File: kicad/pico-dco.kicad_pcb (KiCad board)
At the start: 2 copper layers, 1 part, among them U1 Pico

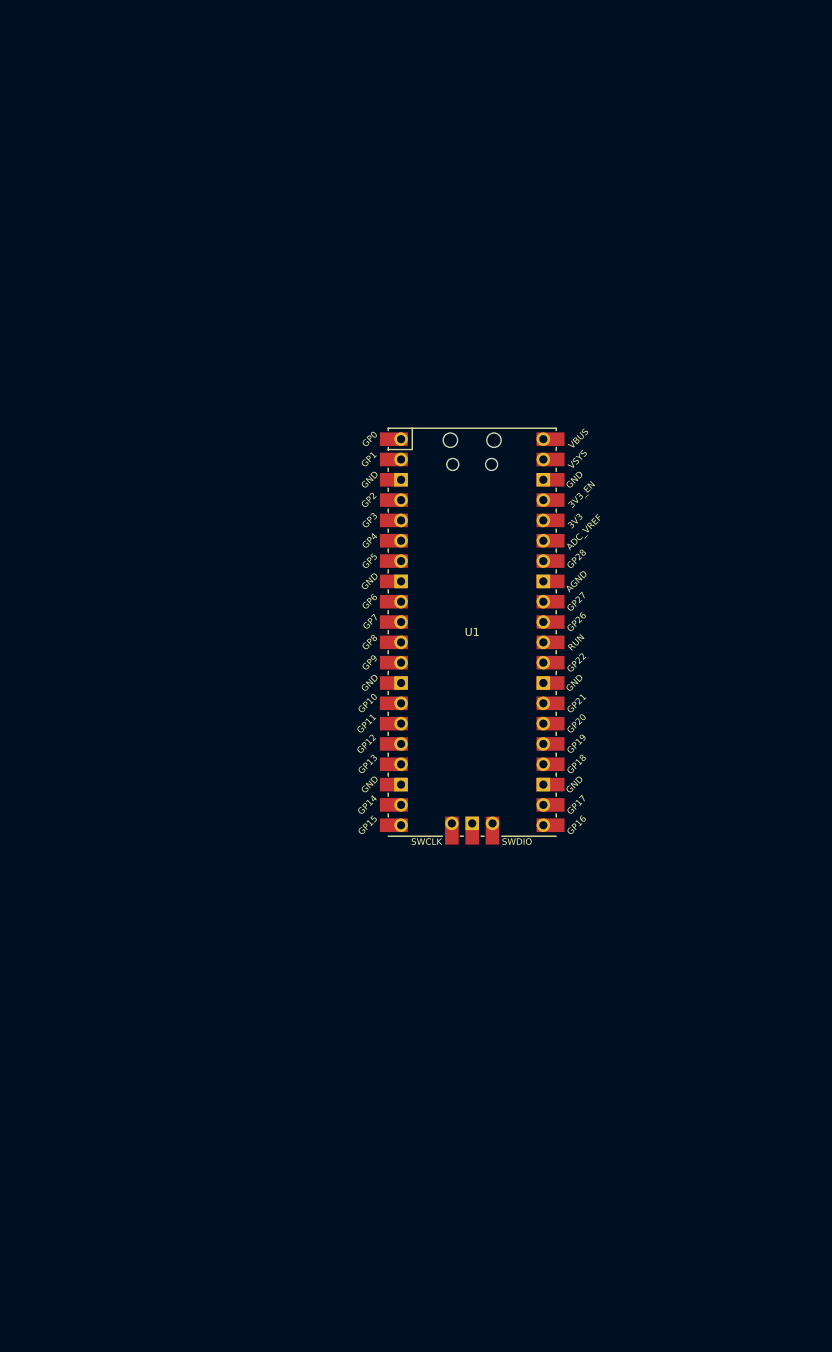
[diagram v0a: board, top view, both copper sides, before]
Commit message: Add 6 voices and serial midi to kicad schematics/PCB
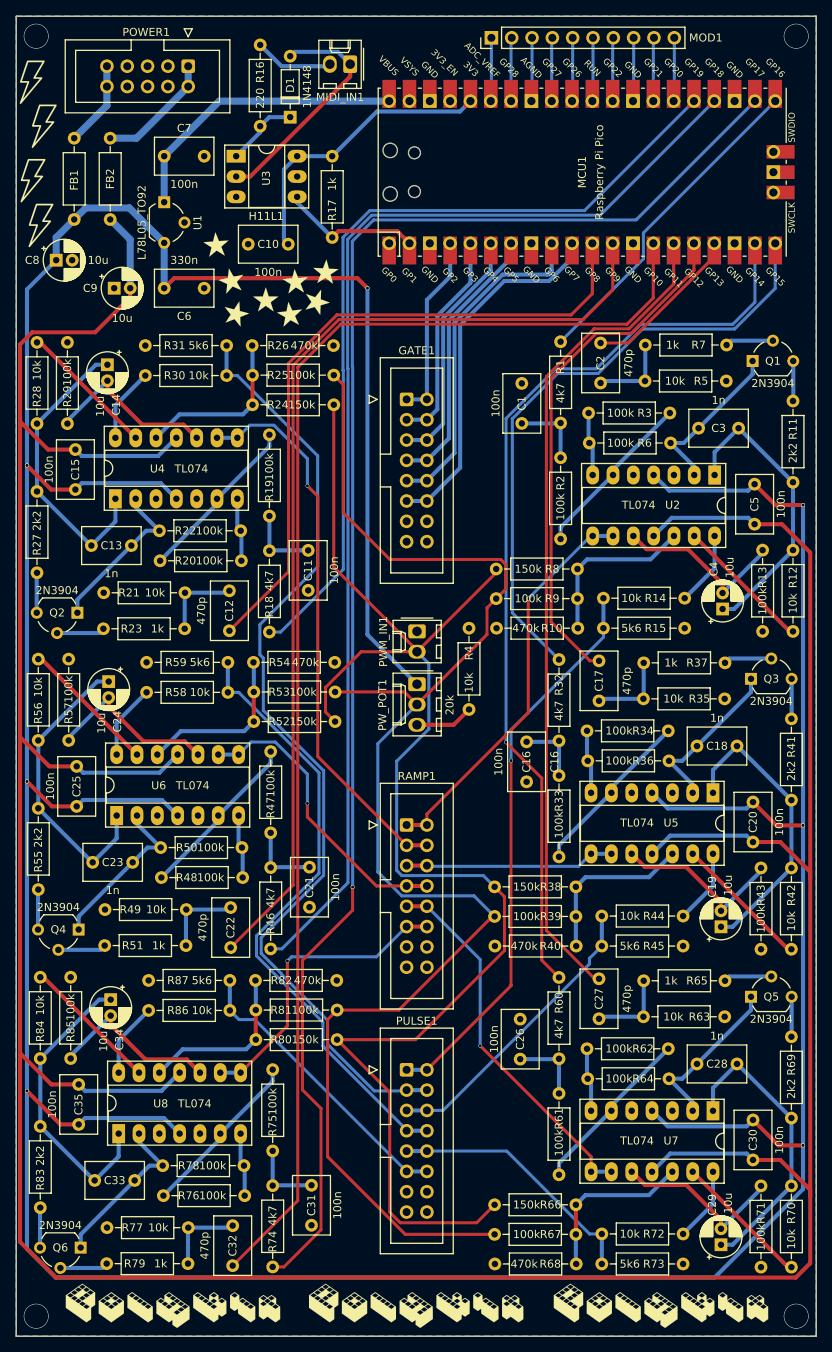
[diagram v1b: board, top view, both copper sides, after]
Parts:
- added C1: 100n, Capacitor_THT:C_Rect_L7.2mm_W4.5mm_P5.00mm_FKS2_FKP2_MKS2_MKP2, F.Cu at (113.2, 70.9)
- added C10: 100n, Capacitor_THT:C_Rect_L7.2mm_W4.5mm_P5.00mm_FKS2_FKP2_MKS2_MKP2, F.Cu at (84.0, 48.5)
- added C11: 100n, Capacitor_THT:C_Rect_L7.2mm_W4.5mm_P5.00mm_FKS2_FKP2_MKS2_MKP2, F.Cu at (86.5, 86.8)
- added C12: 470p, Capacitor_THT:C_Rect_L7.2mm_W4.5mm_P5.00mm_FKS2_FKP2_MKS2_MKP2, F.Cu at (76.7, 91.8)
- added C13: 1n, Capacitor_THT:C_Rect_L7.2mm_W4.5mm_P5.00mm_FKS2_FKP2_MKS2_MKP2, F.Cu at (59.4, 86.2)
- added C14: 10u, Capacitor_THT:CP_Radial_D5.0mm_P2.00mm, F.Cu at (61.4, 63.6)
- added C15: 100n, Capacitor_THT:C_Rect_L7.2mm_W4.5mm_P5.00mm_FKS2_FKP2_MKS2_MKP2, F.Cu at (57.4, 79.2)
- added C16: 100n, Capacitor_THT:C_Rect_L7.2mm_W4.5mm_P5.00mm_FKS2_FKP2_MKS2_MKP2, F.Cu at (113.8, 110.7)
- added C17: 470p, Capacitor_THT:C_Rect_L7.2mm_W4.5mm_P5.00mm_FKS2_FKP2_MKS2_MKP2, F.Cu at (122.8, 105.6)
- added C18: 1n, Capacitor_THT:C_Rect_L7.2mm_W4.5mm_P5.00mm_FKS2_FKP2_MKS2_MKP2, F.Cu at (140.1, 111.2)
- added C19: 10u, Capacitor_THT:CP_Radial_D5.0mm_P2.00mm, F.Cu at (138.1, 133.8)
- added C2: 470p, Capacitor_THT:C_Rect_L7.2mm_W4.5mm_P5.00mm_FKS2_FKP2_MKS2_MKP2, F.Cu at (123.0, 65.8)
- added C20: 100n, Capacitor_THT:C_Rect_L7.2mm_W4.5mm_P5.00mm_FKS2_FKP2_MKS2_MKP2, F.Cu at (142.1, 118.2)
- added C21: 100n, Capacitor_THT:C_Rect_L7.2mm_W4.5mm_P5.00mm_FKS2_FKP2_MKS2_MKP2, F.Cu at (86.7, 126.4)
- added C22: 470p, Capacitor_THT:C_Rect_L7.2mm_W4.5mm_P5.00mm_FKS2_FKP2_MKS2_MKP2, F.Cu at (76.8, 131.4)
- added C23: 1n, Capacitor_THT:C_Rect_L7.2mm_W4.5mm_P5.00mm_FKS2_FKP2_MKS2_MKP2, F.Cu at (59.6, 125.8)
- added C24: 10u, Capacitor_THT:CP_Radial_D5.0mm_P2.00mm, F.Cu at (61.6, 103.2)
- added C25: 100n, Capacitor_THT:C_Rect_L7.2mm_W4.5mm_P5.00mm_FKS2_FKP2_MKS2_MKP2, F.Cu at (57.6, 118.8)
- added C26: 100n, Capacitor_THT:C_Rect_L7.2mm_W4.5mm_P5.00mm_FKS2_FKP2_MKS2_MKP2, F.Cu at (113.0, 150.4)
- added C27: 470p, Capacitor_THT:C_Rect_L7.2mm_W4.5mm_P5.00mm_FKS2_FKP2_MKS2_MKP2, F.Cu at (122.8, 145.3)
- added C28: 1n, Capacitor_THT:C_Rect_L7.2mm_W4.5mm_P5.00mm_FKS2_FKP2_MKS2_MKP2, F.Cu at (140.1, 151.0)
- added C29: 10u, Capacitor_THT:CP_Radial_D5.0mm_P2.00mm, F.Cu at (138.1, 173.6)
- added C3: 1n, Capacitor_THT:C_Rect_L7.2mm_W4.5mm_P5.00mm_FKS2_FKP2_MKS2_MKP2, F.Cu at (140.3, 71.5)
- added C30: 100n, Capacitor_THT:C_Rect_L7.2mm_W4.5mm_P5.00mm_FKS2_FKP2_MKS2_MKP2, F.Cu at (142.1, 158.0)
- added C31: 100n, Capacitor_THT:C_Rect_L7.2mm_W4.5mm_P5.00mm_FKS2_FKP2_MKS2_MKP2, F.Cu at (86.9, 166.1)
- added C32: 470p, Capacitor_THT:C_Rect_L7.2mm_W4.5mm_P5.00mm_FKS2_FKP2_MKS2_MKP2, F.Cu at (77.1, 171.2)
- added C33: 1n, Capacitor_THT:C_Rect_L7.2mm_W4.5mm_P5.00mm_FKS2_FKP2_MKS2_MKP2, F.Cu at (59.8, 165.5)
- added C34: 10u, Capacitor_THT:CP_Radial_D5.0mm_P2.00mm, F.Cu at (61.8, 142.9)
- added C35: 100n, Capacitor_THT:C_Rect_L7.2mm_W4.5mm_P5.00mm_FKS2_FKP2_MKS2_MKP2, F.Cu at (57.8, 158.5)
- added C4: 10u, Capacitor_THT:CP_Radial_D5.0mm_P2.00mm, F.Cu at (138.3, 94.1)
- added C5: 100n, Capacitor_THT:C_Rect_L7.2mm_W4.5mm_P5.00mm_FKS2_FKP2_MKS2_MKP2, F.Cu at (142.3, 78.5)
- added C6: 330n, Capacitor_THT:C_Rect_L7.2mm_W4.5mm_P5.00mm_FKS2_FKP2_MKS2_MKP2, F.Cu at (73.5, 54.0)
- added C7: 100n, Capacitor_THT:C_Rect_L7.2mm_W4.5mm_P5.00mm_FKS2_FKP2_MKS2_MKP2, F.Cu at (68.5, 37.5)
- added C8: 10u, Capacitor_THT:CP_Radial_D5.0mm_P2.00mm, F.Cu at (55.0, 50.5)
- added C9: 10u, Capacitor_THT:CP_Radial_D5.0mm_P2.00mm, F.Cu at (62.2, 54.0)
- added D1: 1N4148, Diode_THT:D_DO-35_SOD27_P7.62mm_Horizontal, F.Cu at (84.2, 32.6)
- added FB1: Ferrite_Bead, Resistor_THT:R_Axial_DIN0207_L6.3mm_D2.5mm_P10.16mm_Horizontal, F.Cu at (57.2, 35.2)
- added FB2: Ferrite_Bead, Resistor_THT:R_Axial_DIN0207_L6.3mm_D2.5mm_P10.16mm_Horizontal, F.Cu at (61.8, 35.2)
- added G***: LOGO, Polykit:star-silk-tiny, F.Cu at (75.0, 48.5)
- added G***: LOGO, Polykit:blitz-silk-tiny, F.Cu at (52.1, 40.6)
- added G***: LOGO, Polykit:blitz-silk-tiny, F.Cu at (53.5, 33.8)
- added G***: LOGO, Polykit:blitz-silk-tiny, F.Cu at (52.0, 28.3)
- added G***: LOGO, Polykit:bär-small, B.Cu at (93.2, 38.7)
- added G***: LOGO, Polykit:logo-silk-2.5cm, F.Cu at (100.0, 181.2)
- added G***: LOGO, Polykit:logo-silk-2.5cm, F.Cu at (130.6, 181.2)
- added G***: LOGO, Polykit:logo-silk-2.5cm, F.Cu at (69.6, 181.2)
- added G***: LOGO, Polykit:star-silk-tiny, F.Cu at (76.9, 53.0)
- added G***: LOGO, Polykit:star-silk-tiny, F.Cu at (77.5, 57.1)
- added G***: LOGO, Polykit:star-silk-tiny, F.Cu at (81.2, 55.4)
- added G***: LOGO, Polykit:star-silk-tiny, F.Cu at (84.9, 53.1)
- added G***: LOGO, Polykit:star-silk-tiny, F.Cu at (84.2, 57.2)
- added G***: LOGO, Polykit:star-silk-tiny, F.Cu at (87.6, 55.6)
- added G***: LOGO, Polykit:star-silk-tiny, F.Cu at (88.7, 51.9)
- added G***: LOGO, Polykit:blitz-silk-tiny, F.Cu at (53.1, 46.2)
- added GATE1: Conn_02x08_Odd_Even, Connector_IDC:IDC-Header_2x08_P2.54mm_Vertical, F.Cu at (98.8, 67.9)
- added MCU1: Raspberry Pi Pico, RPi_Pico:RPi_Pico_SMD_TH, F.Cu at (120.8, 39.5)
- added MIDI_IN1: Conn_01x02, Connector_Molex:Molex_KK-254_AE-6410-02A_1x02_P2.54mm_Vertical, F.Cu at (91.8, 26.0)
- added MOD1: Conn_01x10, Connector_PinHeader_2.54mm:PinHeader_1x10_P2.54mm_Vertical, F.Cu at (109.4, 22.7)
- added POWER1: Conn_02x05_Odd_Even, Connector_IDC:IDC-Header_2x05_P2.54mm_Vertical, F.Cu at (71.5, 26.2)
- added PULSE1: Conn_02x08_Odd_Even, Connector_IDC:IDC-Header_2x08_P2.54mm_Vertical, F.Cu at (98.8, 151.7)
- added PWM_IN1: Conn_01x02, Connector_Molex:Molex_KK-254_AE-6410-02A_1x02_P2.54mm_Vertical, F.Cu at (100.1, 96.9)
- added PW_POT1: 20k, Connector_Molex:Molex_KK-254_AE-6410-03A_1x03_P2.54mm_Vertical, F.Cu at (100.1, 103.5)
- added Q1: 2N3904, Package_TO_SOT_THT:TO-92_Wide, F.Cu at (142.1, 63.1)
- added Q2: 2N3904, Package_TO_SOT_THT:TO-92_Wide, F.Cu at (57.6, 94.6)
- added Q3: 2N3904, Package_TO_SOT_THT:TO-92_Wide, F.Cu at (141.8, 102.8)
- added Q4: 2N3904, Package_TO_SOT_THT:TO-92_Wide, F.Cu at (57.8, 134.2)
- added Q5: 2N3904, Package_TO_SOT_THT:TO-92_Wide, F.Cu at (141.8, 142.6)
- added Q6: 2N3904, Package_TO_SOT_THT:TO-92_Wide, F.Cu at (58.1, 173.9)
- added R1: 4k7, Resistor_THT:R_Axial_DIN0207_L6.3mm_D2.5mm_P10.16mm_Horizontal, F.Cu at (118.0, 70.8)
- added R10: 470k, Resistor_THT:R_Axial_DIN0207_L6.3mm_D2.5mm_P10.16mm_Horizontal, F.Cu at (120.2, 96.5)
- added R11: 2k2, Resistor_THT:R_Axial_DIN0207_L6.3mm_D2.5mm_P10.16mm_Horizontal, F.Cu at (147.1, 68.1)
- added R12: 10k, Resistor_THT:R_Axial_DIN0207_L6.3mm_D2.5mm_P10.16mm_Horizontal, F.Cu at (147.1, 96.9)
- added R13: 100k, Resistor_THT:R_Axial_DIN0207_L6.3mm_D2.5mm_P10.16mm_Horizontal, F.Cu at (143.3, 96.9)
- added R14: 10k, Resistor_THT:R_Axial_DIN0207_L6.3mm_D2.5mm_P10.16mm_Horizontal, F.Cu at (123.4, 92.8)
- added R15: 5k6, Resistor_THT:R_Axial_DIN0207_L6.3mm_D2.5mm_P10.16mm_Horizontal, F.Cu at (123.4, 96.5)
- added R16: 220, Resistor_THT:R_Axial_DIN0207_L6.3mm_D2.5mm_P10.16mm_Horizontal, F.Cu at (80.5, 33.8)
- added R17: 1k, Resistor_THT:R_Axial_DIN0207_L6.3mm_D2.5mm_P10.16mm_Horizontal, F.Cu at (89.5, 37.5)
- added R18: 4k7, Resistor_THT:R_Axial_DIN0207_L6.3mm_D2.5mm_P10.16mm_Horizontal, F.Cu at (81.7, 86.8)
- added R19: 100k, Resistor_THT:R_Axial_DIN0207_L6.3mm_D2.5mm_P10.16mm_Horizontal, F.Cu at (81.7, 72.3)
- added R2: 100k, Resistor_THT:R_Axial_DIN0207_L6.3mm_D2.5mm_P10.16mm_Horizontal, F.Cu at (118.0, 85.3)
- added R20: 100k, Resistor_THT:R_Axial_DIN0207_L6.3mm_D2.5mm_P10.16mm_Horizontal, F.Cu at (78.2, 88.1)
- added R21: 10k, Resistor_THT:R_Axial_DIN0207_L6.3mm_D2.5mm_P10.16mm_Horizontal, F.Cu at (71.1, 92.1)
- added R22: 100k, Resistor_THT:R_Axial_DIN0207_L6.3mm_D2.5mm_P10.16mm_Horizontal, F.Cu at (67.9, 84.3)
- added R23: 1k, Resistor_THT:R_Axial_DIN0207_L6.3mm_D2.5mm_P10.16mm_Horizontal, F.Cu at (60.9, 96.6)
- added R24: 150k, Resistor_THT:R_Axial_DIN0207_L6.3mm_D2.5mm_P10.16mm_Horizontal, F.Cu at (89.7, 68.6)
- added R25: 100k, Resistor_THT:R_Axial_DIN0207_L6.3mm_D2.5mm_P10.16mm_Horizontal, F.Cu at (89.7, 64.9)
- added R26: 470k, Resistor_THT:R_Axial_DIN0207_L6.3mm_D2.5mm_P10.16mm_Horizontal, F.Cu at (79.5, 61.2)
- added R27: 2k2, Resistor_THT:R_Axial_DIN0207_L6.3mm_D2.5mm_P10.16mm_Horizontal, F.Cu at (52.6, 89.6)
- added R28: 10k, Resistor_THT:R_Axial_DIN0207_L6.3mm_D2.5mm_P10.16mm_Horizontal, F.Cu at (52.6, 60.8)
- added R29: 100k, Resistor_THT:R_Axial_DIN0207_L6.3mm_D2.5mm_P10.16mm_Horizontal, F.Cu at (56.4, 60.8)
- added R3: 100k, Resistor_THT:R_Axial_DIN0207_L6.3mm_D2.5mm_P10.16mm_Horizontal, F.Cu at (121.5, 69.6)
- added R30: 10k, Resistor_THT:R_Axial_DIN0207_L6.3mm_D2.5mm_P10.16mm_Horizontal, F.Cu at (76.3, 64.9)
- added R31: 5k6, Resistor_THT:R_Axial_DIN0207_L6.3mm_D2.5mm_P10.16mm_Horizontal, F.Cu at (76.3, 61.2)
- added R32: 4k7, Resistor_THT:R_Axial_DIN0207_L6.3mm_D2.5mm_P10.16mm_Horizontal, F.Cu at (117.8, 110.6)
- added R33: 100k, Resistor_THT:R_Axial_DIN0207_L6.3mm_D2.5mm_P10.16mm_Horizontal, F.Cu at (117.8, 125.1)
- added R34: 100k, Resistor_THT:R_Axial_DIN0207_L6.3mm_D2.5mm_P10.16mm_Horizontal, F.Cu at (121.3, 109.3)
- added R35: 10k, Resistor_THT:R_Axial_DIN0207_L6.3mm_D2.5mm_P10.16mm_Horizontal, F.Cu at (128.4, 105.3)
- added R36: 100k, Resistor_THT:R_Axial_DIN0207_L6.3mm_D2.5mm_P10.16mm_Horizontal, F.Cu at (131.6, 113.1)
- added R37: 1k, Resistor_THT:R_Axial_DIN0207_L6.3mm_D2.5mm_P10.16mm_Horizontal, F.Cu at (138.6, 100.8)
- added R38: 150k, Resistor_THT:R_Axial_DIN0207_L6.3mm_D2.5mm_P10.16mm_Horizontal, F.Cu at (109.8, 128.8)
- added R39: 100k, Resistor_THT:R_Axial_DIN0207_L6.3mm_D2.5mm_P10.16mm_Horizontal, F.Cu at (109.8, 132.5)
- added R4: 10k, Resistor_THT:R_Axial_DIN0207_L6.3mm_D2.5mm_P10.16mm_Horizontal, F.Cu at (106.6, 96.5)
- added R40: 470k, Resistor_THT:R_Axial_DIN0207_L6.3mm_D2.5mm_P10.16mm_Horizontal, F.Cu at (120.0, 136.2)
- added R41: 2k2, Resistor_THT:R_Axial_DIN0207_L6.3mm_D2.5mm_P10.16mm_Horizontal, F.Cu at (146.9, 107.8)
- added R42: 10k, Resistor_THT:R_Axial_DIN0207_L6.3mm_D2.5mm_P10.16mm_Horizontal, F.Cu at (146.9, 136.6)
- added R43: 100k, Resistor_THT:R_Axial_DIN0207_L6.3mm_D2.5mm_P10.16mm_Horizontal, F.Cu at (143.1, 136.6)
- added R44: 10k, Resistor_THT:R_Axial_DIN0207_L6.3mm_D2.5mm_P10.16mm_Horizontal, F.Cu at (123.2, 132.5)
- added R45: 5k6, Resistor_THT:R_Axial_DIN0207_L6.3mm_D2.5mm_P10.16mm_Horizontal, F.Cu at (123.2, 136.2)
- added R46: 4k7, Resistor_THT:R_Axial_DIN0207_L6.3mm_D2.5mm_P10.16mm_Horizontal, F.Cu at (81.8, 126.4)
- added R47: 100k, Resistor_THT:R_Axial_DIN0207_L6.3mm_D2.5mm_P10.16mm_Horizontal, F.Cu at (81.8, 111.9)
- added R48: 100k, Resistor_THT:R_Axial_DIN0207_L6.3mm_D2.5mm_P10.16mm_Horizontal, F.Cu at (78.3, 127.7)
- added R49: 10k, Resistor_THT:R_Axial_DIN0207_L6.3mm_D2.5mm_P10.16mm_Horizontal, F.Cu at (71.3, 131.7)
- added R5: 10k, Resistor_THT:R_Axial_DIN0207_L6.3mm_D2.5mm_P10.16mm_Horizontal, F.Cu at (128.6, 65.6)
- added R50: 100k, Resistor_THT:R_Axial_DIN0207_L6.3mm_D2.5mm_P10.16mm_Horizontal, F.Cu at (68.1, 123.9)
- added R51: 1k, Resistor_THT:R_Axial_DIN0207_L6.3mm_D2.5mm_P10.16mm_Horizontal, F.Cu at (61.1, 136.2)
- added R52: 150k, Resistor_THT:R_Axial_DIN0207_L6.3mm_D2.5mm_P10.16mm_Horizontal, F.Cu at (89.9, 108.2)
- added R53: 100k, Resistor_THT:R_Axial_DIN0207_L6.3mm_D2.5mm_P10.16mm_Horizontal, F.Cu at (89.9, 104.5)
- added R54: 470k, Resistor_THT:R_Axial_DIN0207_L6.3mm_D2.5mm_P10.16mm_Horizontal, F.Cu at (79.7, 100.8)
- added R55: 2k2, Resistor_THT:R_Axial_DIN0207_L6.3mm_D2.5mm_P10.16mm_Horizontal, F.Cu at (52.8, 129.2)
- added R56: 10k, Resistor_THT:R_Axial_DIN0207_L6.3mm_D2.5mm_P10.16mm_Horizontal, F.Cu at (52.8, 100.4)
- added R57: 100k, Resistor_THT:R_Axial_DIN0207_L6.3mm_D2.5mm_P10.16mm_Horizontal, F.Cu at (56.6, 100.4)
- added R58: 10k, Resistor_THT:R_Axial_DIN0207_L6.3mm_D2.5mm_P10.16mm_Horizontal, F.Cu at (76.5, 104.5)
- added R59: 5k6, Resistor_THT:R_Axial_DIN0207_L6.3mm_D2.5mm_P10.16mm_Horizontal, F.Cu at (76.5, 100.8)
- added R6: 100k, Resistor_THT:R_Axial_DIN0207_L6.3mm_D2.5mm_P10.16mm_Horizontal, F.Cu at (131.8, 73.3)
- added R60: 4k7, Resistor_THT:R_Axial_DIN0207_L6.3mm_D2.5mm_P10.16mm_Horizontal, F.Cu at (117.8, 150.3)
- added R61: 100k, Resistor_THT:R_Axial_DIN0207_L6.3mm_D2.5mm_P10.16mm_Horizontal, F.Cu at (117.8, 164.8)
- added R62: 100k, Resistor_THT:R_Axial_DIN0207_L6.3mm_D2.5mm_P10.16mm_Horizontal, F.Cu at (121.3, 149.1)
- added R63: 10k, Resistor_THT:R_Axial_DIN0207_L6.3mm_D2.5mm_P10.16mm_Horizontal, F.Cu at (128.4, 145.1)
- added R64: 100k, Resistor_THT:R_Axial_DIN0207_L6.3mm_D2.5mm_P10.16mm_Horizontal, F.Cu at (131.6, 152.8)
- added R65: 1k, Resistor_THT:R_Axial_DIN0207_L6.3mm_D2.5mm_P10.16mm_Horizontal, F.Cu at (138.6, 140.6)
- added R66: 150k, Resistor_THT:R_Axial_DIN0207_L6.3mm_D2.5mm_P10.16mm_Horizontal, F.Cu at (109.8, 168.6)
- added R67: 100k, Resistor_THT:R_Axial_DIN0207_L6.3mm_D2.5mm_P10.16mm_Horizontal, F.Cu at (109.8, 172.3)
- added R68: 470k, Resistor_THT:R_Axial_DIN0207_L6.3mm_D2.5mm_P10.16mm_Horizontal, F.Cu at (120.0, 176.0)
- added R69: 2k2, Resistor_THT:R_Axial_DIN0207_L6.3mm_D2.5mm_P10.16mm_Horizontal, F.Cu at (146.9, 147.6)
- added R7: 1k, Resistor_THT:R_Axial_DIN0207_L6.3mm_D2.5mm_P10.16mm_Horizontal, F.Cu at (138.8, 61.1)
- added R70: 10k, Resistor_THT:R_Axial_DIN0207_L6.3mm_D2.5mm_P10.16mm_Horizontal, F.Cu at (146.9, 176.4)
- added R71: 100k, Resistor_THT:R_Axial_DIN0207_L6.3mm_D2.5mm_P10.16mm_Horizontal, F.Cu at (143.1, 176.4)
- added R72: 10k, Resistor_THT:R_Axial_DIN0207_L6.3mm_D2.5mm_P10.16mm_Horizontal, F.Cu at (123.2, 172.2)
- added R73: 5k6, Resistor_THT:R_Axial_DIN0207_L6.3mm_D2.5mm_P10.16mm_Horizontal, F.Cu at (123.2, 176.0)
- added R74: 4k7, Resistor_THT:R_Axial_DIN0207_L6.3mm_D2.5mm_P10.16mm_Horizontal, F.Cu at (82.1, 166.2)
- added R75: 100k, Resistor_THT:R_Axial_DIN0207_L6.3mm_D2.5mm_P10.16mm_Horizontal, F.Cu at (82.1, 151.7)
- added R76: 100k, Resistor_THT:R_Axial_DIN0207_L6.3mm_D2.5mm_P10.16mm_Horizontal, F.Cu at (78.6, 167.4)
- added R77: 10k, Resistor_THT:R_Axial_DIN0207_L6.3mm_D2.5mm_P10.16mm_Horizontal, F.Cu at (71.5, 171.4)
- added R78: 100k, Resistor_THT:R_Axial_DIN0207_L6.3mm_D2.5mm_P10.16mm_Horizontal, F.Cu at (68.3, 163.7)
- added R79: 1k, Resistor_THT:R_Axial_DIN0207_L6.3mm_D2.5mm_P10.16mm_Horizontal, F.Cu at (61.3, 175.9)
- added R8: 150k, Resistor_THT:R_Axial_DIN0207_L6.3mm_D2.5mm_P10.16mm_Horizontal, F.Cu at (110.0, 89.1)
- added R80: 150k, Resistor_THT:R_Axial_DIN0207_L6.3mm_D2.5mm_P10.16mm_Horizontal, F.Cu at (90.1, 147.9)
- added R81: 100k, Resistor_THT:R_Axial_DIN0207_L6.3mm_D2.5mm_P10.16mm_Horizontal, F.Cu at (90.1, 144.2)
- added R82: 470k, Resistor_THT:R_Axial_DIN0207_L6.3mm_D2.5mm_P10.16mm_Horizontal, F.Cu at (79.9, 140.5)
- added R83: 2k2, Resistor_THT:R_Axial_DIN0207_L6.3mm_D2.5mm_P10.16mm_Horizontal, F.Cu at (53.0, 168.9)
- added R84: 10k, Resistor_THT:R_Axial_DIN0207_L6.3mm_D2.5mm_P10.16mm_Horizontal, F.Cu at (53.0, 140.1)
- added R85: 100k, Resistor_THT:R_Axial_DIN0207_L6.3mm_D2.5mm_P10.16mm_Horizontal, F.Cu at (56.8, 140.1)
- added R86: 10k, Resistor_THT:R_Axial_DIN0207_L6.3mm_D2.5mm_P10.16mm_Horizontal, F.Cu at (76.7, 144.3)
- added R87: 5k6, Resistor_THT:R_Axial_DIN0207_L6.3mm_D2.5mm_P10.16mm_Horizontal, F.Cu at (76.7, 140.5)
- added R9: 100k, Resistor_THT:R_Axial_DIN0207_L6.3mm_D2.5mm_P10.16mm_Horizontal, F.Cu at (110.0, 92.8)
- added RAMP1: Conn_02x08_Odd_Even, Connector_IDC:IDC-Header_2x08_P2.54mm_Vertical, F.Cu at (98.8, 121.1)
- added U2: TL074, Package_DIP:DIP-14_W7.62mm_Socket_LongPads, F.Cu at (137.3, 77.3)
- added U3: H11L1, Package_DIP:DIP-6_W7.62mm_Socket_LongPads, F.Cu at (77.5, 37.5)
- added U4: TL074, Package_DIP:DIP-14_W7.62mm_Socket_LongPads, F.Cu at (62.4, 80.3)
- added U5: TL074, Package_DIP:DIP-14_W7.62mm_Socket_LongPads, F.Cu at (137.1, 117.1)
- added U6: TL074, Package_DIP:DIP-14_W7.62mm_Socket_LongPads, F.Cu at (62.6, 119.9)
- added U7: TL074, Package_DIP:DIP-14_W7.62mm_Socket_LongPads, F.Cu at (137.1, 156.8)
- added U8: TL074, Package_DIP:DIP-14_W7.62mm_Socket_LongPads, F.Cu at (62.8, 159.7)
- U1: value Pico -> L78L05_TO92; footprint RPi_Pico:RPi_Pico_SMD_TH -> Package_TO_SOT_THT:TO-92_Wide
- moved U1 66.1 mm to (68.5, 43.2), turned to 270 degrees
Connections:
- U1 pad 1: Net-(U1-Pad1) -> +5V
- U1 pad 2: Net-(U1-Pad2) -> GND
- U1 pad 3: Net-(U1-Pad3) -> +12V
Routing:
- net +12V: track 0.00 -> 545.3 mm, vias 0 -> 7
- net -12V: track 0.00 -> 466.7 mm
- net RANGE_PWM5: track 0.00 -> 192.7 mm, vias 0 -> 1
- net PWM_IN: track 0.00 -> 183.3 mm
- net PW_POT: track 0.00 -> 181.8 mm
- net RESET5: track 0.00 -> 170.5 mm
- net RANGE_PWM3: track 0.00 -> 146.5 mm
- net RESET3: track 0.00 -> 125.7 mm
- net PULSE_OUT1: track 0.00 -> 120.7 mm
- net RANGE_PWM4: track 0.00 -> 117.1 mm, vias 0 -> 1
- net RANGE_PWM1: track 0.00 -> 104.9 mm
- net RESET4: track 0.00 -> 104.1 mm
- net RESET1: track 0.00 -> 84.4 mm
- net RANGE_PWM2: track 0.00 -> 77.8 mm
- net PULSE_OUT3: track 0.00 -> 77.6 mm
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- added copper zone on B.Cu, net GND
- added copper zone on F.Cu, net GND
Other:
- board outline added: 100 x 165 mm
- board text added: "Polykit Raspberry Pi Pico DCO v2.0.0 Jan Knipper 2021 github.com/polykit/pico-dco"

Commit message: Update silk screen
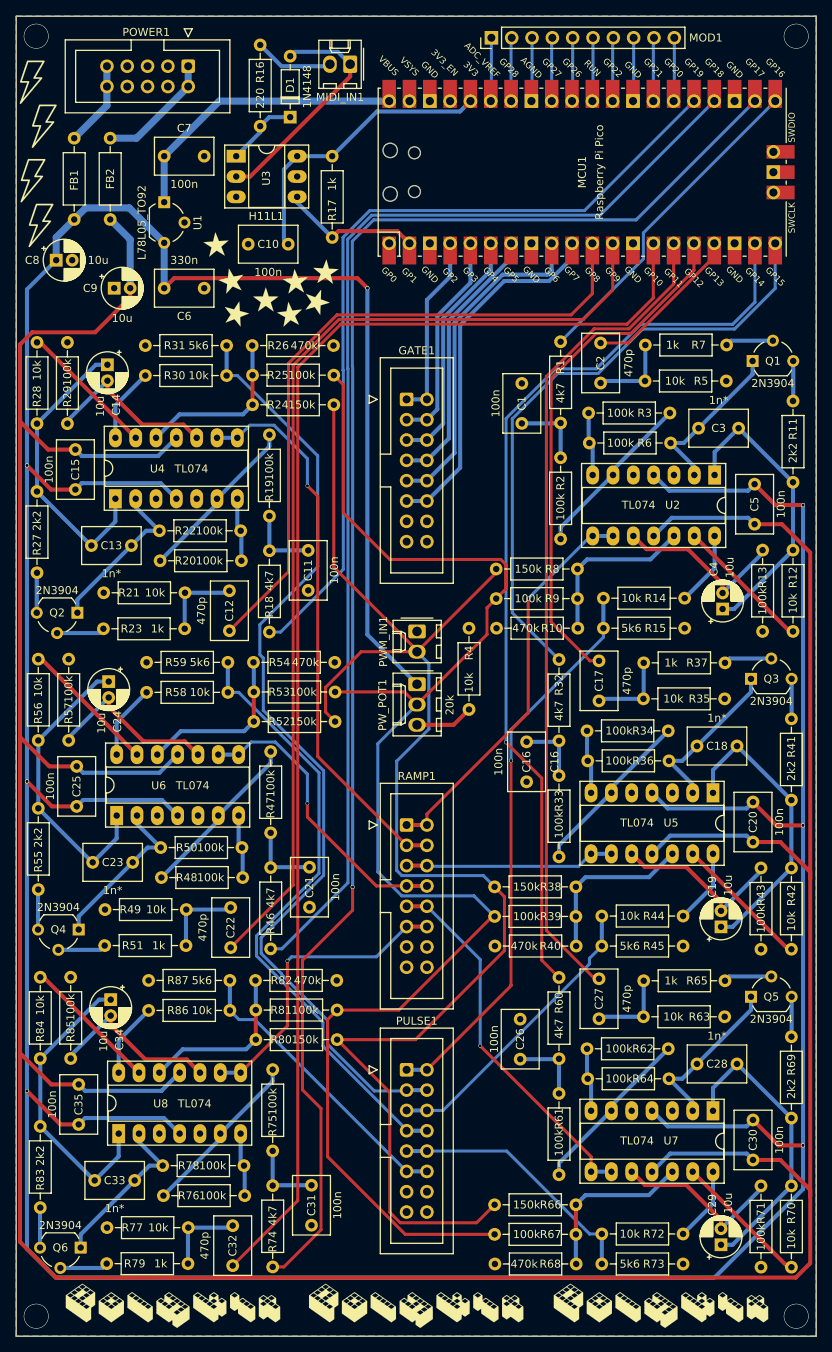
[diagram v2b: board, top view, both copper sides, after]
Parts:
- C13, C18, C23, C28, C3, C33: value 1n -> 1n*
- moved G*** 0.30 mm to (93.5, 38.7)
